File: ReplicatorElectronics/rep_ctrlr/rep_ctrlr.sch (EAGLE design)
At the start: 65 parts, among them IC1 MICROCHIP_PIC32MX7X5F256L-PF, IC2 MICROCHIP_MCP6001-LT, IC3 MICROCHIP_MCP6001-LT, IC4 MICROCHIP_MCP6001-LT, IC5 MICROCHIP_MCP6001-LT, IC6 LT1963E-3.3Q, J1 ATX24RH, J10 SBH21-NBPN-D05-ST-BK, J11 SBH21-NBPN-D07-ST-BK, J12 SBH21-NBPN-D07-ST-BK, J13 SBH21-NBPN-D07-ST-BK, J14 SBH21-NBPN-D07-ST-BK, J15 SBH21-NBPN-D07-ST-BK, J3 FPS009-30003, J4 SBH21-NBPN-D05-ST-BK, J5 SBH21-NBPN-D05-ST-BK, J6 SBH21-NBPN-D07-ST-BK, J7 SBH21-NBPN-D07-ST-BK, J8 SBH21-NBPN-D05-ST-BK, J9 SBH21-NBPN-D07-ST-BK

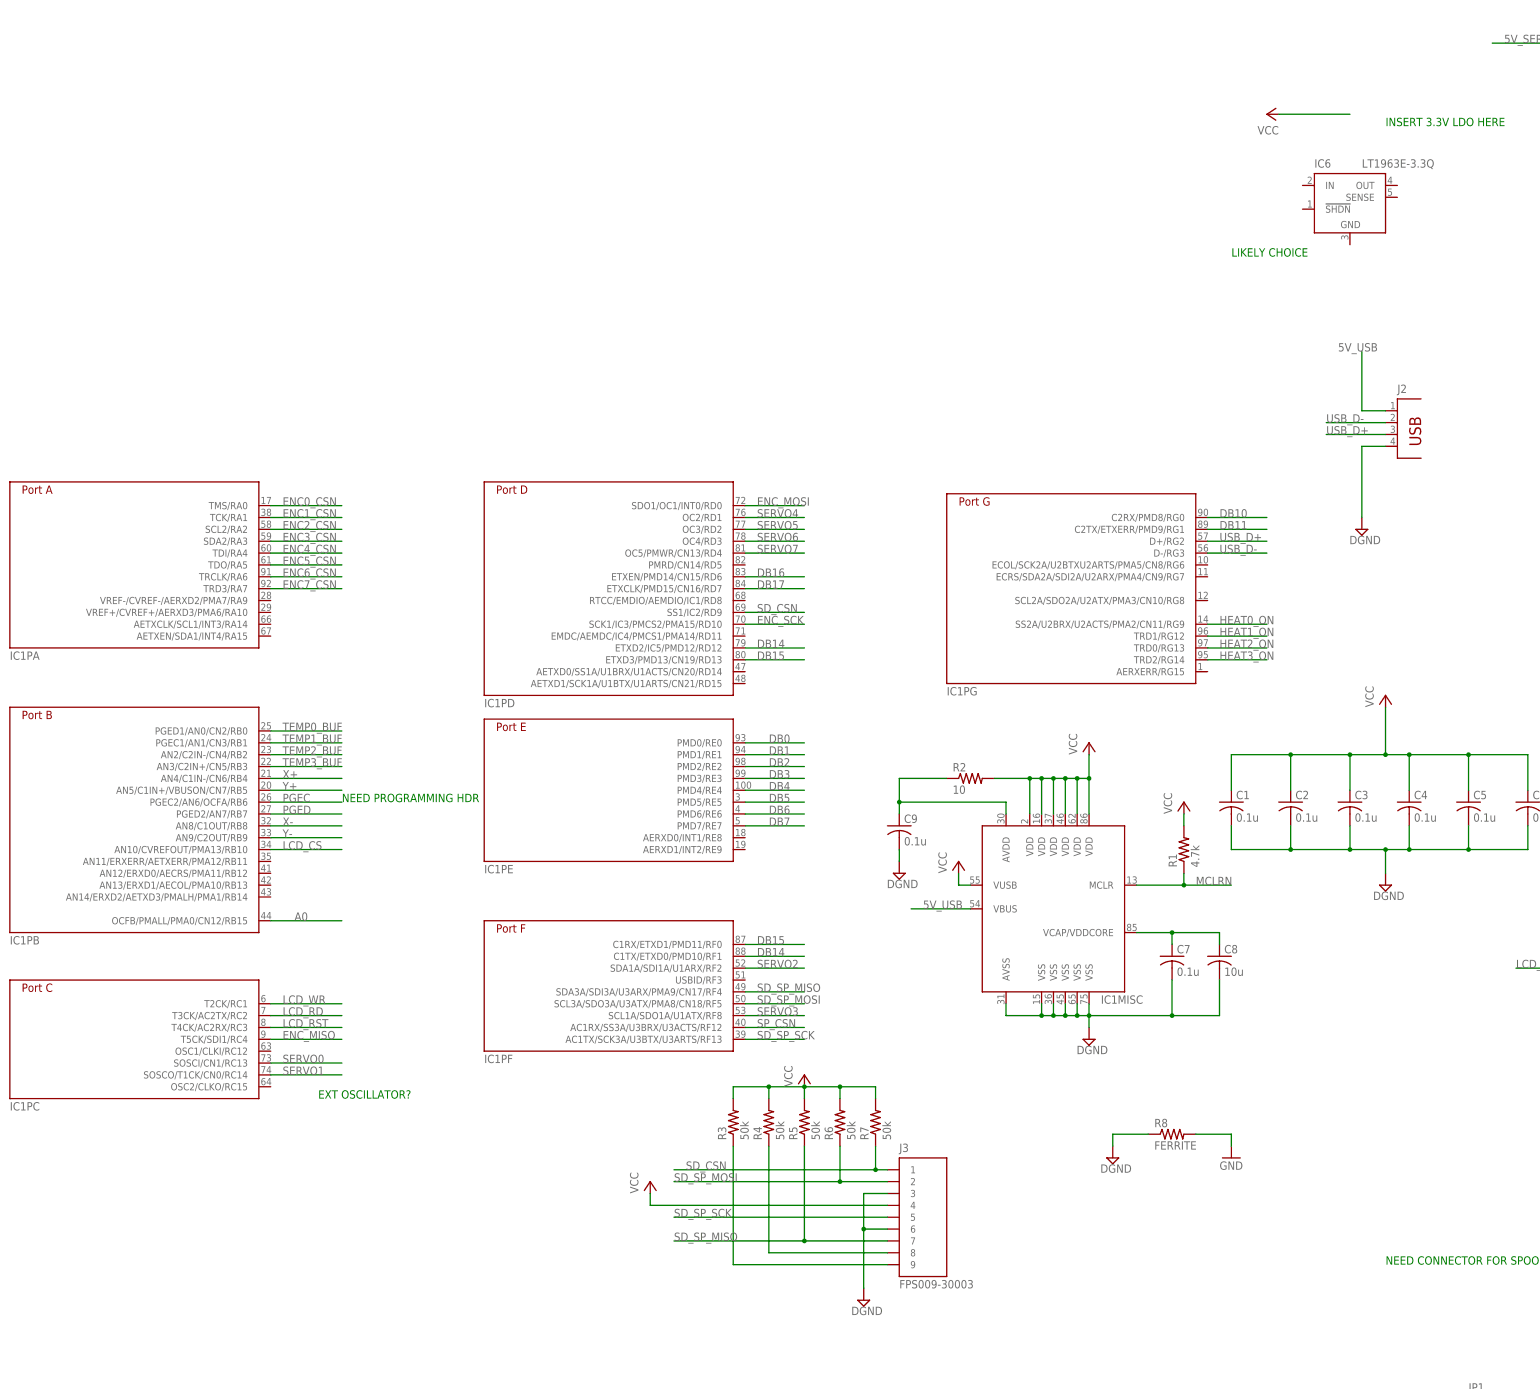
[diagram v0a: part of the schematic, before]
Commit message: added reg and xtal
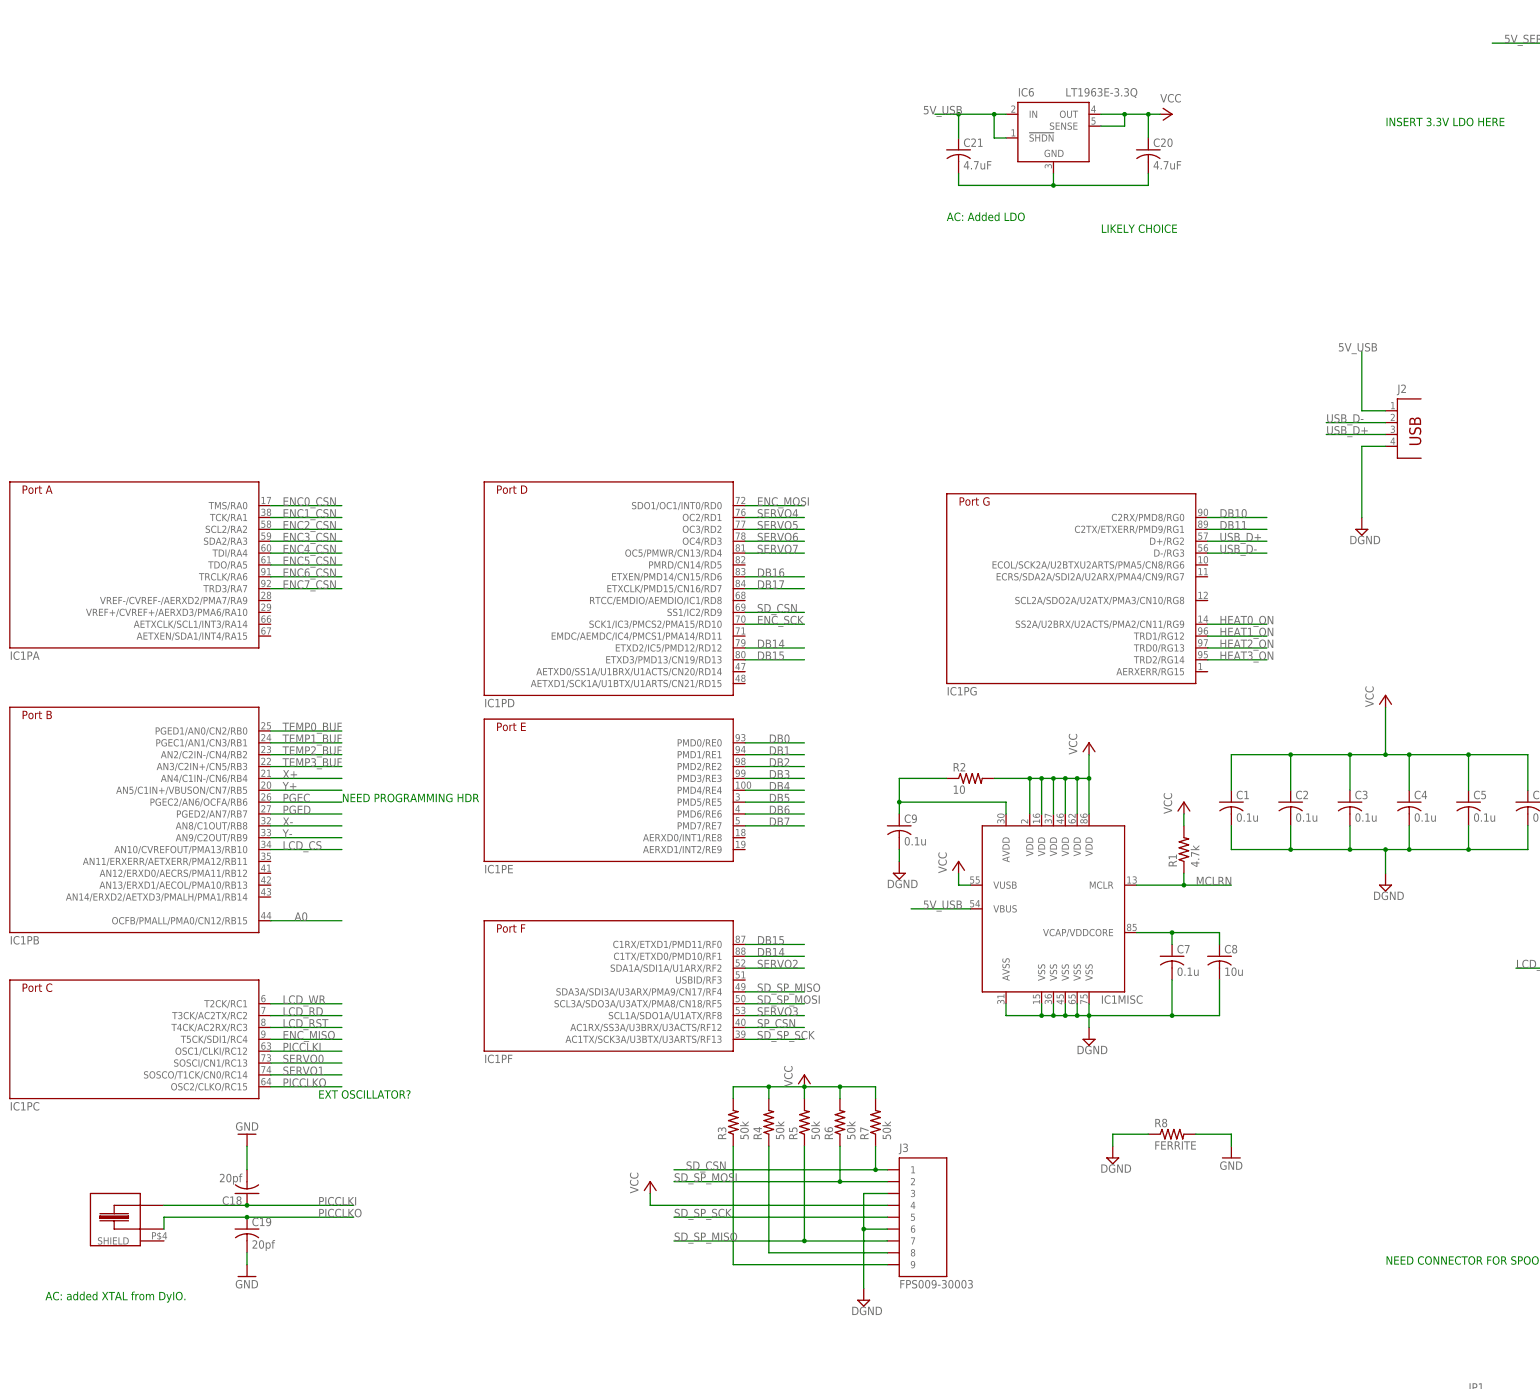
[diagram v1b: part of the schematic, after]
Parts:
- added C18, C19: 20pf, rcl:C-USC0603
- added C20, C21: 4.7uF, resistor:C-USC0603
- added X2: CMR3XXT, cmr3XXT:CMR3XXT
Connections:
- new net N$22: C20.2, C21.2, IC6.GND
- new net PICCLKI: C18.1, IC1PC.OSC1/CLKI/RC12, X2.P$1
- new net PICCLKO: C19.1, IC1PC.OSC2/CLKO/RC15, X2.P$2
- net 5V_USB: now also C21.1, IC6.!SHDN, IC6.IN
- net GND: now also C18.2, C19.2
- net VCC: now also C20.1, IC6.SENSE
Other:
- note added: "AC: Added LDO"
- note added: "AC: added XTAL from DyIO."
- moved on the sheet: IC6
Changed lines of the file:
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@@
 <part name="GND14" library="supply1" deviceset="GND" device=""/>
 <part name="IC6" library="linear-technology" deviceset="LT1963E" device="Q" technology="-3.3"/>
+<part name="GND15" library="supply1" deviceset="GND" device=""/>
+<part name="GND16" library="supply1" deviceset="GND" device=""/>
+<part name="C18" library="rcl" deviceset="C-US" device="C0603" value="20pf"/>
+<part name="C19" library="rcl" deviceset="C-US" device="C0603" value="20pf"/>
+<part name="X2" library="cmr3XXT" deviceset="CMR3XXT" device=""/>
+<part name="C20" library="resistor" deviceset="C-US" device="C0603" value="4.7uF"/>
+<part name="C21" library="resistor" deviceset="C-US" device="C0603" value="4.7uF"/>
 </parts>
 <sheets>
@@
 <text x="609.6" y="40.64" size="1.778" layer="91">ASSUMING 10K THERMISTOR</text>
 <text x="617.22" y="-104.14" size="1.778" layer="91">ASSUMING 10K THERMISTOR</text>
-<text x="142.24" y="27.94" size="1.778" layer="91">LIKELY CHOICE</text>
+<text x="114.3" y="33.02" size="1.778" layer="91">LIKELY CHOICE</text>
 <text x="-53.34" y="-152.4" size="1.778" layer="91">EXT OSCILLATOR?</text>
 <text x="-48.26" y="-88.9" size="1.778" layer="91">NEED PROGRAMMING HDR</text>
+<text x="-111.76" y="-195.58" size="1.778" layer="91">AC: added XTAL from DyIO.</text>
+<text x="81.28" y="35.56" size="1.778" layer="91">AC: Added LDO</text>
 </plain>
 <instances>
@@
 <instance part="P+6" gate="VCC" x="50.8" y="-147.32"/>
 <instance part="P+7" gate="VCC" x="17.78" y="-170.18"/>
-<instance part="P+4" gate="VCC" x="149.86" y="58.42" rot="R90"/>
+<instance part="P+4" gate="VCC" x="129.54" y="58.42" rot="R270"/>
 <instance part="SUPPLY1" gate="G$1" x="71.12" y="-104.14"/>
 <instance part="SUPPLY2" gate="G$1" x="63.5" y="-195.58"/>
@@
 <instance part="SUPPLY36" gate="G$1" x="927.1" y="-259.08"/>
 <instance part="GND14" gate="1" x="927.1" y="-243.84"/>
-<instance part="IC6" gate="G$1" x="167.64" y="40.64"/>
+<instance part="IC6" gate="G$1" x="104.14" y="55.88"/>
+<instance part="GND15" gate="1" x="-68.58" y="-160.02" rot="R180"/>
+<instance part="GND16" gate="1" x="-68.58" y="-190.5"/>
+<instance part="C18" gate="G$1" x="-68.58" y="-172.72" rot="R180"/>
+<instance part="C19" gate="G$1" x="-68.58" y="-180.34"/>
+<instance part="X2" gate="G$1" x="-86.36" y="-182.88" rot="MR0"/>
+<instance part="C20" gate="G$1" x="124.46" y="50.8"/>
+<instance part="C21" gate="G$1" x="83.82" y="50.8"/>
 </instances>
 <busses>
@@
 <segment>
 <pinref part="P+4" gate="VCC" pin="VCC"/>
-<wire x1="152.4" y1="58.42" x2="167.64" y2="58.42" width="0.1524" layer="91"/>
+<wire x1="127" y1="58.42" x2="124.46" y2="58.42" width="0.1524" layer="91"/>
+<pinref part="IC6" gate="G$1" pin="SENSE"/>
+<wire x1="124.46" y1="58.42" x2="119.38" y2="58.42" width="0.1524" layer="91"/>
+<wire x1="119.38" y1="58.42" x2="114.3" y2="58.42" width="0.1524" layer="91"/>
+<wire x1="114.3" y1="55.88" x2="119.38" y2="55.88" width="0.1524" layer="91"/>
+<wire x1="119.38" y1="55.88" x2="119.38" y2="58.42" width="0.1524" layer="91"/>
+<junction x="119.38" y="58.42"/>
+<pinref part="C20" gate="G$1" pin="1"/>
+<wire x1="124.46" y1="53.34" x2="124.46" y2="58.42" width="0.1524" layer="91"/>
+<junction x="124.46" y="58.42"/>
 </segment>
 <segment>
@@
 <pinref part="GND14" gate="1" pin="GND"/>
 </segment>
+<segment>
+<wire x1="-68.58" y1="-187.96" x2="-68.58" y2="-185.42" width="0.1524" layer="91"/>
+<pinref part="GND16" gate="1" pin="GND"/>
+<pinref part="C19" gate="G$1" pin="2"/>
+</segment>
+<segment>
+<wire x1="-68.58" y1="-162.56" x2="-68.58" y2="-167.64" width="0.1524" layer="91"/>
+<pinref part="GND15" gate="1" pin="GND"/>
+<pinref part="C18" gate="G$1" pin="2"/>
+</segment>
 </net>
 <net name="N$5" class="0">
@@
 <wire x1="170.18" y1="-5.08" x2="170.18" y2="7.62" width="0.1524" layer="91"/>
 <label x="165.1" y="7.62" size="1.778" layer="95"/>
+</segment>
+<segment>
+<pinref part="IC6" gate="G$1" pin="IN"/>
+<wire x1="93.98" y1="58.42" x2="91.44" y2="58.42" width="0.1524" layer="91"/>
+<pinref part="IC6" gate="G$1" pin="!SHDN"/>
+<wire x1="91.44" y1="58.42" x2="83.82" y2="58.42" width="0.1524" layer="91"/>
+<wire x1="83.82" y1="58.42" x2="78.74" y2="58.42" width="0.1524" layer="91"/>
+<wire x1="93.98" y1="53.34" x2="91.44" y2="53.34" width="0.1524" layer="91"/>
+<wire x1="91.44" y1="53.34" x2="91.44" y2="58.42" width="0.1524" layer="91"/>
+<junction x="91.44" y="58.42"/>
+<label x="76.2" y="58.42" size="1.778" layer="95"/>
+<pinref part="C21" gate="G$1" pin="1"/>
+<wire x1="83.82" y1="53.34" x2="83.82" y2="58.42" width="0.1524" layer="91"/>
+<junction x="83.82" y="58.42"/>
 </segment>
 </net>
@@
 </segment>
 </net>
+<net name="PICCLKO" class="0">
+<segment>
+<wire x1="-68.58" y1="-177.8" x2="-86.36" y2="-177.8" width="0.1524" layer="91"/>
+<wire x1="-86.36" y1="-177.8" x2="-86.36" y2="-180.34" width="0.1524" layer="91"/>
+<wire x1="-45.72" y1="-177.8" x2="-68.58" y2="-177.8" width="0.1524" layer="91"/>
+<junction x="-68.58" y="-177.8"/>
+<pinref part="X2" gate="G$1" pin="P$2"/>
+<pinref part="C19" gate="G$1" pin="1"/>
+<label x="-53.34" y="-177.8" size="1.778" layer="95"/>
+</segment>
+<segment>
+<pinref part="IC1" gate="PC" pin="OSC2/CLKO/RC15"/>
+<wire x1="-63.5" y1="-149.86" x2="-48.26" y2="-149.86" width="0.1524" layer="91"/>
+<label x="-60.96" y="-149.86" size="1.778" layer="95"/>
+</segment>
+</net>
+<net name="PICCLKI" class="0">
+<segment>
+<wire x1="-68.58" y1="-175.26" x2="-86.36" y2="-175.26" width="0.1524" layer="91"/>
+<wire x1="-68.58" y1="-175.26" x2="-45.72" y2="-175.26" width="0.1524" layer="91"/>
+<junction x="-68.58" y="-175.26"/>
+<pinref part="X2" gate="G$1" pin="P$1"/>
+<pinref part="C18" gate="G$1" pin="1"/>
+<label x="-53.34" y="-175.26" size="1.778" layer="95"/>
+</segment>
+<segment>
+<pinref part="IC1" gate="PC" pin="OSC1/CLKI/RC12"/>
+<wire x1="-63.5" y1="-142.24" x2="-48.26" y2="-142.24" width="0.1524" layer="91"/>
+<label x="-60.96" y="-142.24" size="1.778" layer="95"/>
+</segment>
+</net>
+<net name="N$22" class="0">
+<segment>
+<pinref part="C21" gate="G$1" pin="2"/>
+<wire x1="83.82" y1="45.72" x2="83.82" y2="43.18" width="0.1524" layer="91"/>
+<pinref part="C20" gate="G$1" pin="2"/>
+<wire x1="83.82" y1="43.18" x2="104.14" y2="43.18" width="0.1524" layer="91"/>
+<wire x1="104.14" y1="43.18" x2="124.46" y2="43.18" width="0.1524" layer="91"/>
+<wire x1="124.46" y1="43.18" x2="124.46" y2="45.72" width="0.1524" layer="91"/>
+<pinref part="IC6" gate="G$1" pin="GND"/>
+<wire x1="104.14" y1="45.72" x2="104.14" y2="43.18" width="0.1524" layer="91"/>
+<junction x="104.14" y="43.18"/>
+</segment>
+</net>

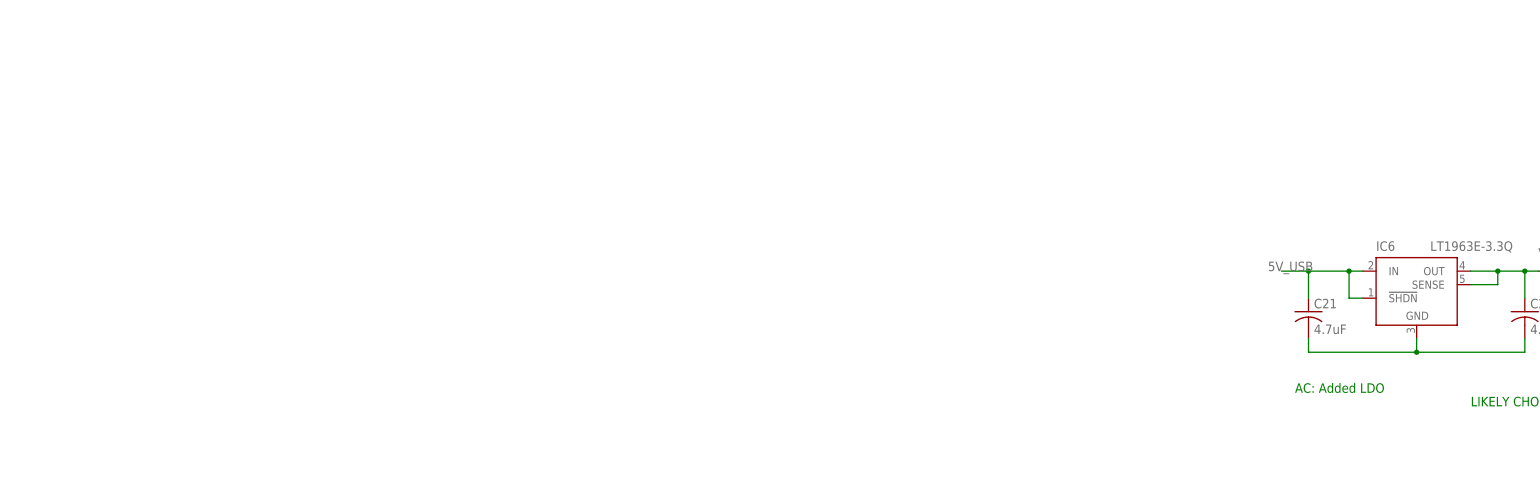
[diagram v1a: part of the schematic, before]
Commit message: started wiring the PHY
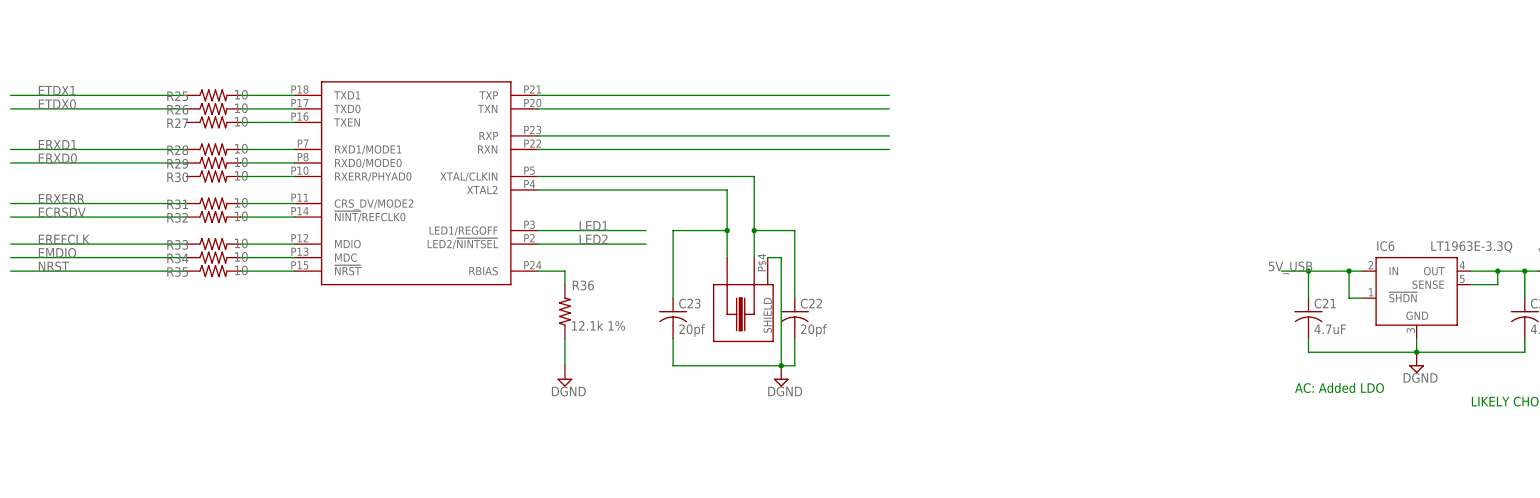
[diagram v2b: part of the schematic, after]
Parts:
- added C22, C23: 20pf, rcl:C-USC0603
- added R25, R26, R27, R28, R29, R30, R31, R32, R33, R34, R35: 10, resistor:R-US_R0603
- added R36: 12.1k 1%, resistor:R-US_R0603
- added U$2: 8720A_PHY, SMSC8720a_Ethernet_PHY:8720A_PHY
- added X1: CMR3XXT, cmr3XXT:CMR3XXT
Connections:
- removed net N$22: C20.2, C21.2, IC6.GND
- new net ECRSDV: R32.1
- new net EMDIO: R34.1
- new net EREFCLK: R33.1
- new net ERXD0: R29.1
- new net ERXD1: R28.1
- new net ERXERR: R31.1
- new net ETDX0: R26.1
- new net ETDX1: R25.1
- new net LED1: U$2G$1.LED1/REGOFF
- new net LED2: U$2G$1.LED2/!NINTSEL
- new net N$23: R25.2, U$2G$1.TXD1
- new net N$24: R26.2, U$2G$1.TXD0
- new net N$25: R27.2, U$2G$1.TXEN
- new net N$26: R28.2, U$2G$1.RXD1/MODE1
- new net N$27: R29.2, U$2G$1.RXD0/MODE0
- new net N$28: R30.2, U$2G$1.RXERR/PHYAD0
- new net N$29: R31.2, U$2G$1.CRS_DV/MODE2
- new net N$30: R32.2, U$2G$1.!NINT/!REFCLK0
- new net N$31: R33.2, U$2G$1.MDIO
- new net N$32: R34.2, U$2G$1.MDC
- new net N$33: R35.2, U$2G$1.!NRST
- new net N$34: U$2G$1.TXP
- new net N$35: U$2G$1.TXN
- new net N$36: U$2G$1.RXP
- new net N$37: U$2G$1.RXN
- new net N$38: C22.1, U$2G$1.XTAL/CLKIN, X1.P$2
- new net N$39: C23.1, U$2G$1.XTAL2, X1.P$1
- new net N$52: R36.2, U$2G$1.RBIAS
- new net NRST: R35.1
- net DGND: now also C20.2, C21.2, C22.2, C23.2, IC6.GND, R36.1, X1.SHIELD
